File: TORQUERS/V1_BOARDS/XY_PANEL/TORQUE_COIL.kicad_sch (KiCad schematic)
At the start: 39 parts, among them Q1 BSS138, Q2 BSS138, Q4 BSS138, Q5 BSS138, U1 DRV8830DGQ

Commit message: made changes according to feedback
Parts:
- removed C2: 10uF, Capacitor_SMD:C_0805_2012Metric, symbol SparkFun-Capacitor:C_Polarized
- added C2: CL21A106KOQNNNE, CAPC2012X140N, symbol AA_AUTO_LOADER:CL21A106KOQNNNE
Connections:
- net GND: now also C2.1
- net at C?.1, D7.1 (K), D8.1 (K)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: now also C2.2
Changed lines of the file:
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@@
   (junction (at 224.536 58.166) (diameter 0) (color 0 0 0 0)
   )
+  (junction (at 136.144 75.692) (diameter 0) (color 0 0 0 0)
+  )
   (junction (at 219.456 23.876) (diameter 0) (color 0 0 0 0)
   )
-  (junction (at 156.464 77.978) (diameter 0) (color 0 0 0 0)
-  )
   (junction (at 219.456 31.496) (diameter 0) (color 0 0 0 0)
   )
@@
   (junction (at 135.382 75.184) (diameter 0) (color 0 0 0 0)
   )
-  (junction (at 156.21 77.978) (diameter 0) (color 0 0 0 0)
-  )
   (junction (at 257.556 70.866) (diameter 0) (color 0 0 0 0)
   )
@@
   (junction (at 61.214 93.98) (diameter 0) (color 0 0 0 0)
   )
+  (junction (at 156.972 75.692) (diameter 0) (color 0 0 0 0)
+  )
   (junction (at 61.214 88.9) (diameter 0) (color 0 0 0 0)
   )
@@
   )
   (junction (at 66.294 88.392) (diameter 0) (color 0 0 0 0)
-  )
-  (junction (at 136.144 77.978) (diameter 0) (color 0 0 0 0)
   )
   (junction (at 135.382 71.12) (diameter 0) (color 0 0 0 0)
@@
     (stroke (width 0) (type default))
   )
+  (wire (pts (xy 136.144 75.692) (xy 136.144 77.978))
+    (stroke (width 0) (type default))
+  )
   (wire (pts (xy 61.214 93.98) (xy 61.214 96.774))
     (stroke (width 0) (type default))
@@
     (stroke (width 0) (type default))
   )
+  (wire (pts (xy 156.464 90.424) (xy 156.464 92.456))
+    (stroke (width 0) (type default))
+  )
   (wire (pts (xy 244.856 48.006) (xy 234.696 48.006))
     (stroke (width 0) (type default))
@@
     (stroke (width 0) (type default))
   )
-  (wire (pts (xy 156.21 77.978) (xy 156.464 77.978))
-    (stroke (width 0) (type default))
-  )
   (wire (pts (xy 252.73 71.12) (xy 254 71.12))
     (stroke (width 0) (type default))
@@
     (stroke (width 0) (type default))
   )
+  (wire (pts (xy 156.972 75.692) (xy 136.144 75.692))
+    (stroke (width 0) (type default))
+  )
   (wire (pts (xy 143.256 71.374) (xy 143.764 71.374))
     (stroke (width 0) (type default))
@@
     (stroke (width 0) (type default))
   )
-  (wire (pts (xy 156.21 78.232) (xy 156.464 78.232))
-    (stroke (width 0) (type default))
-  )
   (wire (pts (xy 213.106 53.086) (xy 214.376 53.086))
     (stroke (width 0) (type default))
@@
     (stroke (width 0) (type default))
   )
+  (wire (pts (xy 156.972 88.392) (xy 156.972 90.424))
+    (stroke (width 0) (type default))
+  )
   (wire (pts (xy 143.002 71.12) (xy 143.256 71.12))
     (stroke (width 0) (type default))
@@
     (stroke (width 0) (type default))
   )
-  (wire (pts (xy 136.144 75.184) (xy 136.144 77.978))
+  (wire (pts (xy 136.144 75.184) (xy 136.144 75.692))
     (stroke (width 0) (type default))
   )
@@
     (stroke (width 0) (type default))
   )
+  (wire (pts (xy 156.972 90.424) (xy 156.464 90.424))
+    (stroke (width 0) (type default))
+  )
   (wire (pts (xy 66.294 88.138) (xy 87.376 88.138))
     (stroke (width 0) (type default))
@@
     (stroke (width 0) (type default))
   )
-  (wire (pts (xy 156.464 85.598) (xy 156.464 92.456))
-    (stroke (width 0) (type default))
-  )
   (wire (pts (xy 135.382 71.12) (xy 135.382 75.184))
     (stroke (width 0) (type default))
@@
     (stroke (width 0) (type default))
   )
-  (wire (pts (xy 156.21 78.232) (xy 156.21 77.978))
-    (stroke (width 0) (type default))
-  )
-  (wire (pts (xy 156.464 77.978) (xy 165.862 77.978))
-    (stroke (width 0) (type default))
-  )
   (wire (pts (xy 61.976 82.55) (xy 63.754 82.55))
     (stroke (width 0) (type default))
@@
     (stroke (width 0) (type default))
   )
+  (wire (pts (xy 165.862 75.692) (xy 156.972 75.692))
+    (stroke (width 0) (type default))
+  )
   (wire (pts (xy 252.476 50.546) (xy 252.476 48.006))
     (stroke (width 0) (type default))
@@
     (stroke (width 0) (type default))
   )
+  (wire (pts (xy 165.862 77.978) (xy 165.862 75.692))
+    (stroke (width 0) (type default))
+  )
   (wire (pts (xy 257.556 63.246) (xy 257.556 58.166))
     (stroke (width 0) (type default))
@@
   )
   (wire (pts (xy 127.762 71.12) (xy 127.254 71.12))
-    (stroke (width 0) (type default))
-  )
-  (wire (pts (xy 136.144 77.978) (xy 156.21 77.978))
     (stroke (width 0) (type default))
   )
@@
         (path "/97119169-578f-44be-8822-faf8f0e4fcd6/6ee29482-1d20-4563-80a8-1ef8780df18b"
           (reference "#PWR013") (unit 1)
-        )
-      )
-    )
-  )
-  (symbol (lib_id "SparkFun-Capacitor:C_Polarized") (at 156.464 81.788 0) (unit 1)
-    (in_bom yes) (on_board yes) (dnp no)
-    (property "Reference" "C2" (at 148.844 74.676 0)
-      (effects (font (size 1.27 1.27)) (justify left))
-    )
-    (property "Value" "10uF" (at 148.844 77.216 0)
-      (effects (font (size 1.27 1.27)) (justify left))
-    )
-    (property "Footprint" "Capacitor_SMD:C_0805_2012Metric" (at 156.464 81.788 0)
-      (effects (font (size 1.27 1.27)) hide)
-    )
-    (property "Datasheet" "[link text](https://cdn.sparkfun.com/assets/8/a/4/a/5/Kemet_Capacitor_Datasheet.pdf)" (at 157.734 97.028 0)
-      (effects (font (size 1.27 1.27)) hide)
-    )
-    (property "PROD_ID" "CAP-00000" (at 156.464 94.488 0)
-      (effects (font (size 1.27 1.27)) hide)
-    )
-    (property "Tolerance" "100%" (at 148.844 79.756 0)
-      (effects (font (size 1.27 1.27)) (justify left))
-    )
-    (property "Voltage" "1kV" (at 148.844 82.296 0)
-      (effects (font (size 1.27 1.27)) (justify left))
-    )
-    (pin "1")
-    (pin "2")
-    (instances
-      (project "Xpanel_V1_final"
-        (path "/97119169-578f-44be-8822-faf8f0e4fcd6"
-          (reference "C2") (unit 1)
-        )
-        (path "/97119169-578f-44be-8822-faf8f0e4fcd6/db306d3f-1ab7-4e38-afab-c78bdb56c587"
-          (reference "C6") (unit 1)
-        )
-        (path "/97119169-578f-44be-8822-faf8f0e4fcd6/6ee29482-1d20-4563-80a8-1ef8780df18b"
-          (reference "C6") (unit 1)
         )
       )
@@
         )
       )
+    )
+  )
+  (symbol (lib_id "AA_AUTO_LOADER:CL21A106KOQNNNE") (at 156.972 88.392 90) (unit 1)
+    (in_bom yes) (on_board yes) (dnp no) (fields_autoplaced)
+    (property "Reference" "C2" (at 160.528 80.772 90)
+      (effects (font (size 1.27 1.27)) (justify right))
+    )
+    (property "Value" "CL21A106KOQNNNE" (at 160.528 83.312 90)
+      (effects (font (size 1.27 1.27)) (justify right))
+    )
+    (property "Footprint" "CAPC2012X140N" (at 155.702 79.502 0)
+      (effects (font (size 1.27 1.27)) (justify left) hide)
+    )
+    (property "Datasheet" "https://datasheet.datasheetarchive.com/originals/distributors/Datasheets_SAMA/0289c6d4f30f89b64e7dd5b6a9ee99f0.pdf" (at 158.242 79.502 0)
+      (effects (font (size 1.27 1.27)) (justify left) hide)
+    )
+    (property "Description" "Samsung Electro-Mechanics 0805 (2012M) 10uF MLCC 16V dc +/-10% SMD CL21A106KOQNNNE" (at 160.782 79.502 0)
+      (effects (font (size 1.27 1.27)) (justify left) hide)
+    )
+    (property "Height" "1.4" (at 163.322 79.502 0)
+      (effects (font (size 1.27 1.27)) (justify left) hide)
+    )
+    (property "Manufacturer_Name" "SAMSUNG" (at 165.862 79.502 0)
+      (effects (font (size 1.27 1.27)) (justify left) hide)
+    )
+    (property "Manufacturer_Part_Number" "CL21A106KOQNNNE" (at 168.402 79.502 0)
+      (effects (font (size 1.27 1.27)) (justify left) hide)
+    )
+    (property "Mouser Part Number" "187-CL21A106KOQNNNE" (at 170.942 79.502 0)
+      (effects (font (size 1.27 1.27)) (justify left) hide)
+    )
+    (property "Mouser Price/Stock" "https://www.mouser.co.uk/ProductDetail/Samsung-Electro-Mechanics/CL21A106KOQNNNE?qs=349EhDEZ59qKIX0T0PKtPw%3D%3D" (at 173.482 79.502 0)
+      (effects (font (size 1.27 1.27)) (justify left) hide)
+    )
+    (property "Arrow Part Number" "CL21A106KOQNNNE" (at 176.022 79.502 0)
+      (effects (font (size 1.27 1.27)) (justify left) hide)
+    )
+    (property "Arrow Price/Stock" "https://www.arrow.com/en/products/cl21a106koqnnne/samsung-electro-mechanics?region=nac" (at 178.562 79.502 0)
+      (effects (font (size 1.27 1.27)) (justify left) hide)
+    )
+    (pin "1")
+    (pin "2")
+    (instances
+      (project "Xpanel_V1_final"
+        (path "/97119169-578f-44be-8822-faf8f0e4fcd6/6ee29482-1d20-4563-80a8-1ef8780df18b"
+          (reference "C2") (unit 1)
+        )
+      )

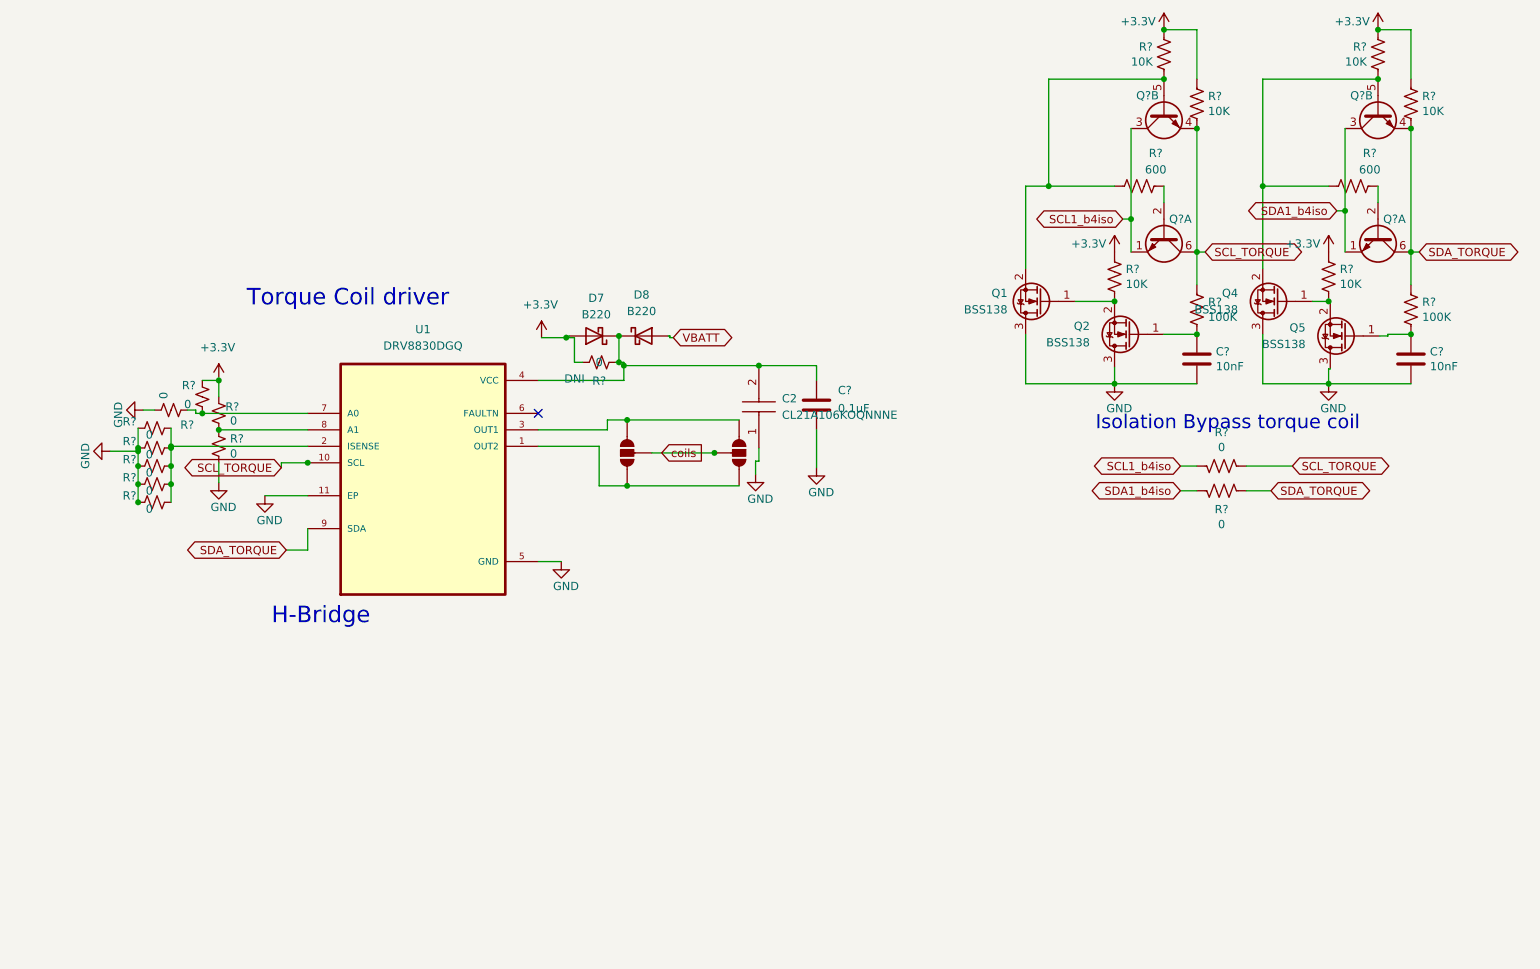
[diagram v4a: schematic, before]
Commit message: added buck for coil driver
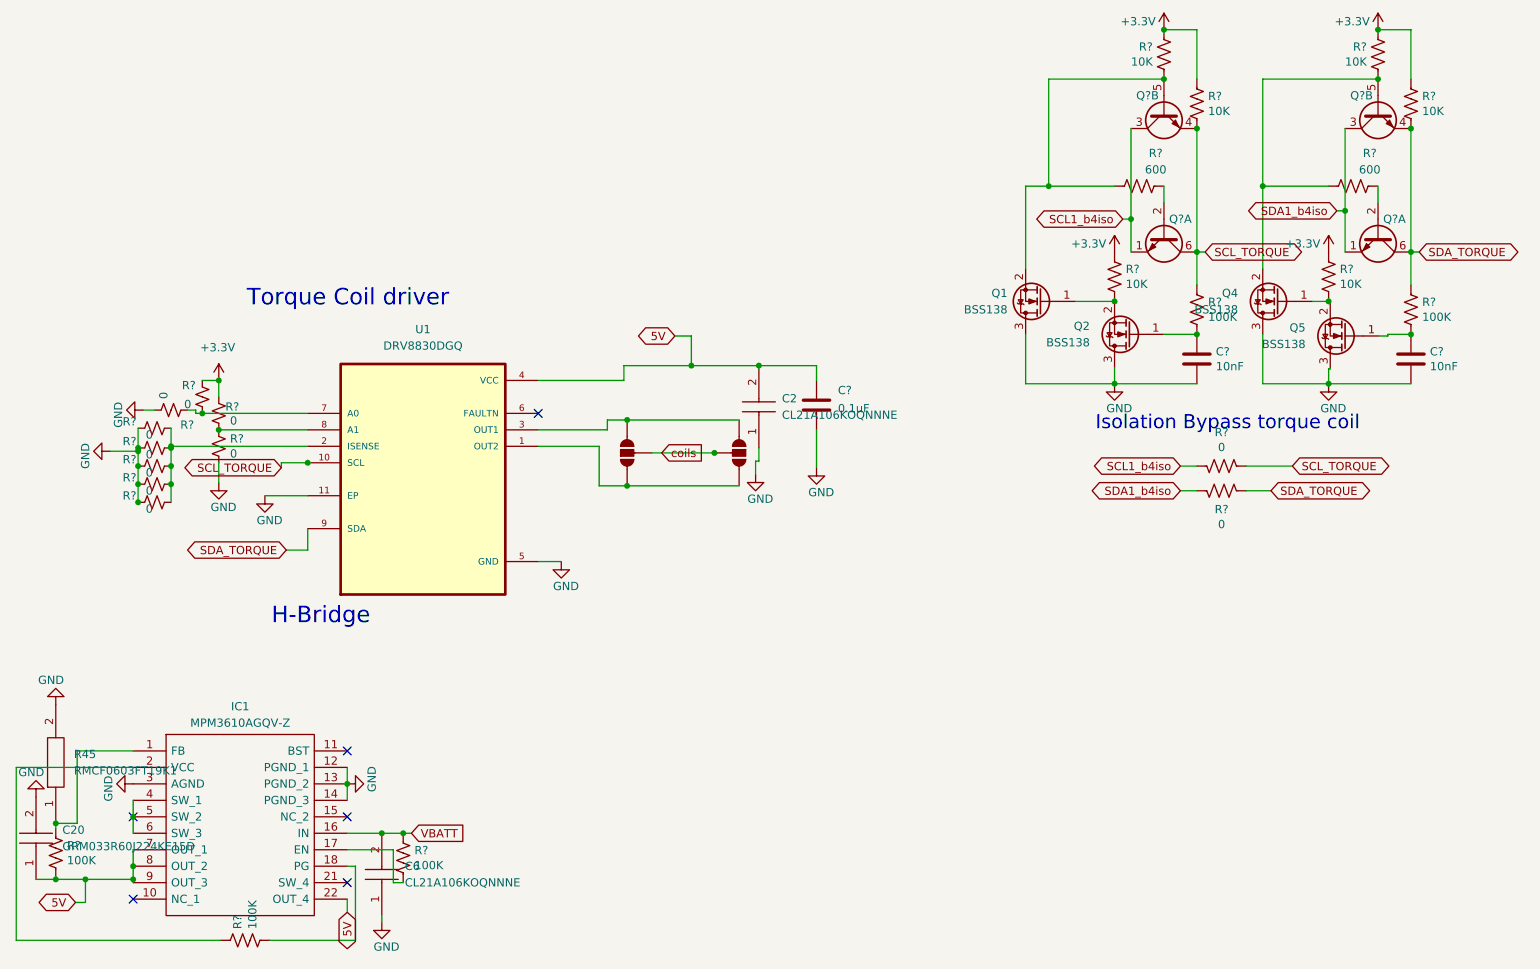
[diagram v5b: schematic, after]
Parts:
- removed D7, D8: B220, Diode_SMD:D_SMB, symbol Diode:B220
- removed R?: 0, Resistor_SMD:R_0603_1608Metric, symbol Device:R_Small_US
- added C20: GRM033R60J224KE15D, CAPC0603X33N, symbol AA_AUTO_LOADER:GRM033R60J224KE15D
- added C6: CL21A106KOQNNNE, CAPC2012X140N, symbol AA_AUTO_LOADER:CL21A106KOQNNNE
- added IC1: MPM3610AGQV-Z, MPM3610AGQVZ, symbol AA_AUTO_LOADER:MPM3610AGQV-Z
- added R45: RMCF0603FT19K1, RESC1608X55N, symbol AA_AUTO_LOADER:RMCF0603FT19K1
- added R? (x3): 100K, Resistor_SMD:R_0603_1608Metric, symbol Device:R_US
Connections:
- net GND: now also C20.2, C6.1, IC1.12 (PGND_1), IC1.13 (PGND_2), IC1.14 (PGND_3), IC1.3 (AGND), R45.2
- net VBATT: now also C6.2, IC1.16 (IN), R?.2
- net 5V: now reaches C2.2, C?.1, U1.4 (VCC)
- net 5V: now also C20.1, IC1.22 (OUT_4), IC1.7 (OUT_1), IC1.8 (OUT_2), IC1.9 (OUT_3), R?.1
- new net: IC1.17 (EN), R?.1
- new net: IC1.1 (FB), R45.1, R?.2
- new net: IC1.18 (PG), R?.1
- new net: IC1.2 (VCC), R?.2
- new net: IC1.4 (SW_1), IC1.5 (SW_2), IC1.6 (SW_3)
- no-connect marks 1 -> 6

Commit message: final push XY board with step updated
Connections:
- net nc: now reaches IC1.21 (SW_4)
- net nc: now also IC1.4 (SW_1), IC1.5 (SW_2), IC1.6 (SW_3)
- no-connect marks 6 -> 4
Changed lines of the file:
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@@
   (junction (at 87.376 90.678) (diameter 0) (color 0 0 0 0)
   )
-  (junction (at 60.452 145.288) (diameter 0) (color 0 0 0 0)
-  )
   (junction (at 201.676 48.006) (diameter 0) (color 0 0 0 0)
   )
@@
   )
   (junction (at 257.556 58.166) (diameter 0) (color 0 0 0 0)
+  )
+  (junction (at 58.674 145.288) (diameter 0) (color 0 0 0 0)
   )
   (junction (at 66.294 88.392) (diameter 0) (color 0 0 0 0)
@@
   (no_connect (at 60.452 157.988))
   (no_connect (at 93.472 135.128))
-  (no_connect (at 93.472 155.448))
   (no_connect (at 122.936 83.058))
-  (no_connect (at 60.452 145.288))
   (wire (pts (xy 42.418 137.668) (xy 60.452 137.668))
     (stroke (width 0) (type default))
@@
     (stroke (width 0) (type default))
   )
-  (wire (pts (xy 60.452 142.748) (xy 60.452 145.288))
-    (stroke (width 0) (type default))
-  )
   (wire (pts (xy 48.514 146.304) (xy 48.514 147.066))
     (stroke (width 0) (type default))
@@
     (stroke (width 0) (type default))
   )
+  (wire (pts (xy 58.674 142.748) (xy 58.674 145.288))
+    (stroke (width 0) (type default))
+  )
   (wire (pts (xy 211.836 78.486) (xy 211.836 75.946))
     (stroke (width 0) (type default))
@@
     (stroke (width 0) (type default))
   )
-  (wire (pts (xy 60.452 145.288) (xy 60.452 147.828))
+  (wire (pts (xy 58.674 145.288) (xy 58.674 147.828))
     (stroke (width 0) (type default))
   )
@@
     (stroke (width 0) (type default))
   )
+  (wire (pts (xy 60.452 142.748) (xy 58.674 142.748))
+    (stroke (width 0) (type default))
+  )
   (wire (pts (xy 87.376 104.14) (xy 87.376 100.838))
     (stroke (width 0) (type default))
   )
+  (wire (pts (xy 58.674 145.288) (xy 60.452 145.288))
+    (stroke (width 0) (type default))
+  )
   (wire (pts (xy 146.558 75.692) (xy 136.144 75.692))
     (stroke (width 0) (type default))
@@
     (stroke (width 0) (type default))
   )
+  (wire (pts (xy 93.472 155.448) (xy 94.234 155.448))
+    (stroke (width 0) (type default))
+  )
   (wire (pts (xy 93.472 152.908) (xy 94.742 152.908))
     (stroke (width 0) (type default))
@@
   )
   (wire (pts (xy 70.104 83.058) (xy 71.12 83.058))
+    (stroke (width 0) (type default))
+  )
+  (wire (pts (xy 58.674 147.828) (xy 60.452 147.828))
     (stroke (width 0) (type default))
   )
@@
     (effects (font (size 2.54 2.54)) (justify left bottom))
   )
+  (label "nc" (at 93.98 155.448 0) (fields_autoplaced)
+    (effects (font (size 1.27 1.27)) (justify left bottom))
+  )
+  (label "nc" (at 58.674 145.288 90) (fields_autoplaced)
+    (effects (font (size 1.27 1.27)) (justify left bottom))
+  )
   (global_label "5V" (shape bidirectional) (at 144.018 71.12 180)
